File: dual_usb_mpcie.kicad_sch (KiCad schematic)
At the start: 28 parts, among them J1 91304-56-052R2, J2 91304-56-052R2, J3 USB, U1 AZ1117H-3.3, U2 AZ1117H-3.3, U3 AZ1117H-1.5, U4 AZ1117H-1.5

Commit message: Remove 1.5v. Change bottom pour to shield. Couple shield with ground. Add pull-up to W_DIS and PCIE_RST.
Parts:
- removed C5, C6: 22uF, Capacitor_SMD:C_1206_3216Metric, symbol Device:C_Polarized_Small_US
- removed FID1, FID2, FID3: Fiducial, parts:fiducial_jlcpcb_smt, symbol Mechanical:Fiducial
- removed U3, U4: AZ1117H-1.5, Package_TO_SOT_SMD:SOT-223-3_TabPin2, symbol Regulator_Linear:AZ1117-1.5
- added C5, C6, C7: 0.1uF, Capacitor_SMD:C_0603_1608Metric, symbol Device:C_Small
- added R3: 1M, Resistor_SMD:R_0603_1608Metric, symbol Device:R_Small_US
- added R4, R5, R6, R7: 3.3k, Resistor_SMD:R_0603_1608Metric, symbol Device:R_Small_US
- C1, C2, C3, C4: symbol Device:C_Polarized_Small_US -> Device:C_Small
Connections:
- net +3.3V_A: now also R6.1, R7.1
- net +3.3V_B: now also R4.1, R5.1
- net GND: now also C5.2, C6.2, C7.2, R3.2; no longer H1.1, H2.1, H3.1, H4.1
- net at J1.20 (~{W_DISABLE}): now also R6.2
- net at J1.22 (~{PERST}): now also C6.1, R7.2
- net at J2.20 (~{W_DISABLE}): now also R4.2
- net at J2.22 (~{PERST}): now also C5.1, R5.2
- net SHIELD: now reaches J3.10 (Pin_10)
- net SHIELD: now also H1.1, H2.1, H3.1, H4.1, C7.1, R3.1
- removed net +1.5V_A: J1.28 (+1V5), J1.48 (+1V5), J1.6 (+1V5)
- removed net +1.5V_B: J2.28 (+1V5), J2.48 (+1V5), J2.6 (+1V5)
- no-connect marks 52 -> 53

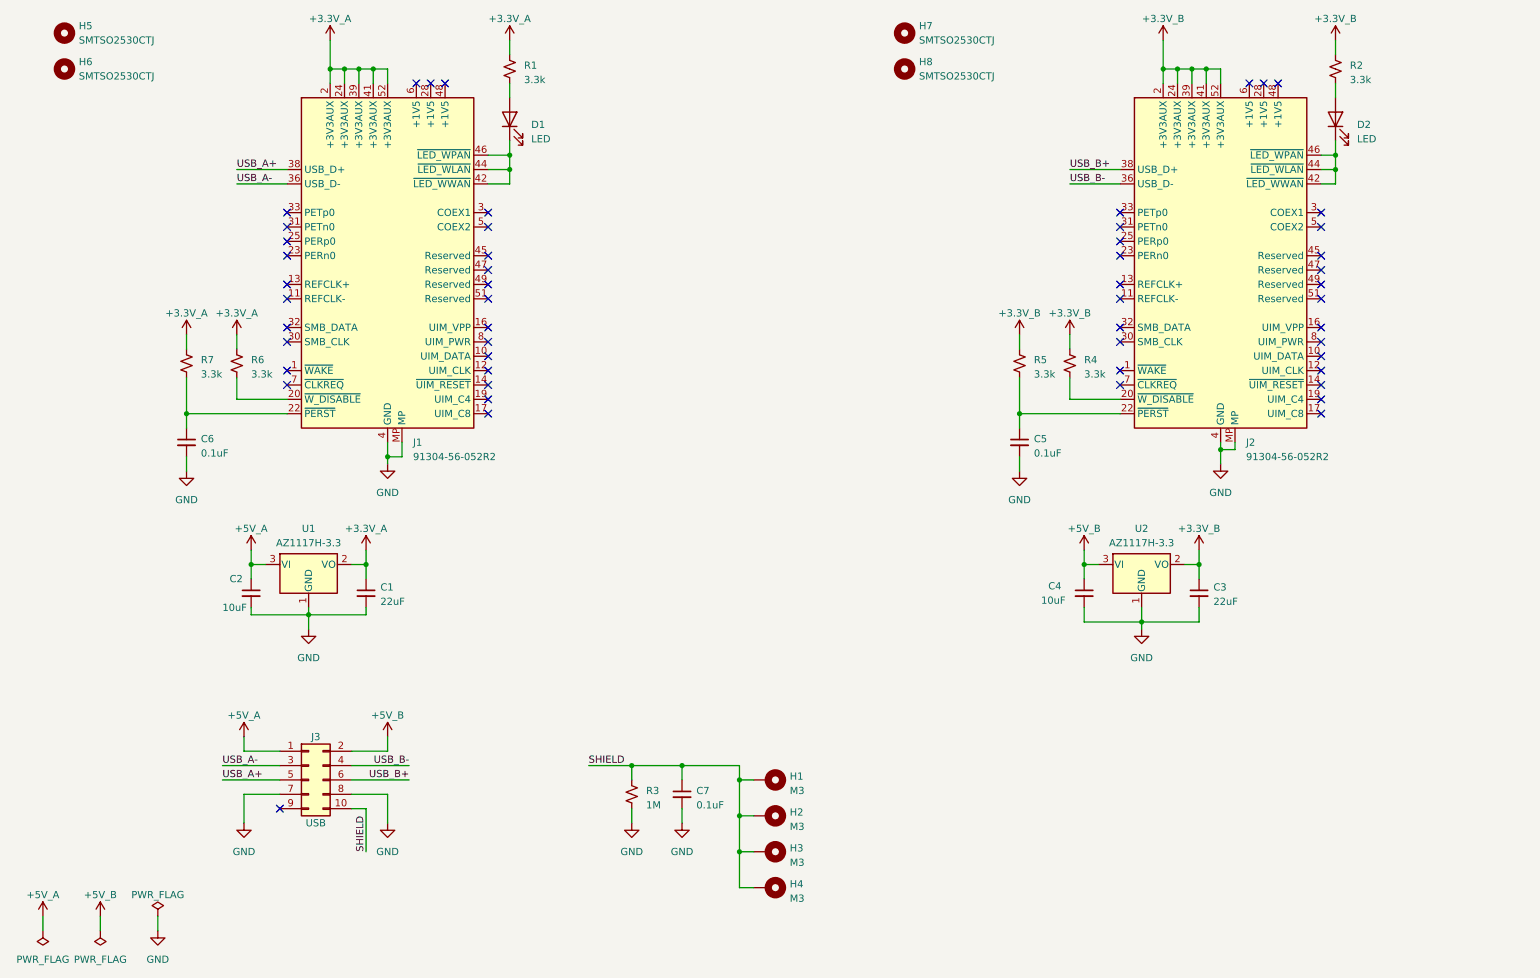
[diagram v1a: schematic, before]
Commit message: Rotate mpcie connectors so all routing is at the top of the board. Move power to the top. Move up mpcie connectors. Add silkscreen. Add models to mpcie and standoff
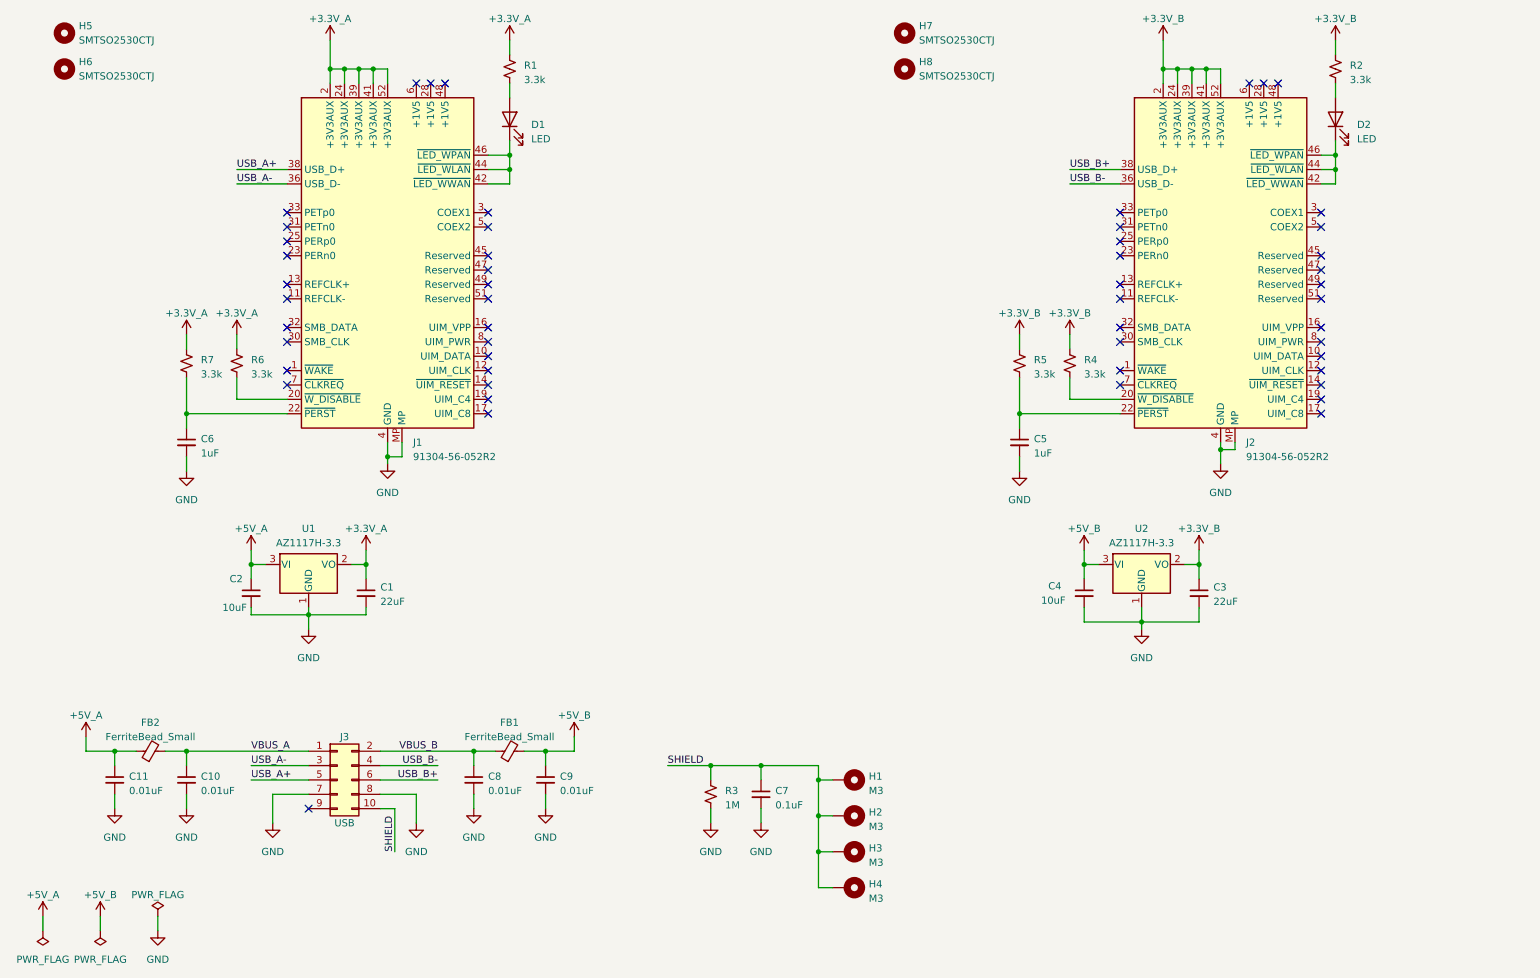
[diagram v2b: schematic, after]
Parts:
- added C10, C11, C8, C9: 0.01uF, Capacitor_SMD:C_0603_1608Metric, symbol Device:C_Small
- added FB1, FB2: FerriteBead_Small, Inductor_SMD:L_0603_1608Metric, symbol Device:FerriteBead_Small
- C5, C6: value 0.1uF -> 1uF; LCSC C14663 -> C15849
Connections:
- net +5V_A: now also C11.1, FB2.1; no longer J3.1 (Pin_1)
- net +5V_B: now also C9.1, FB1.2; no longer J3.2 (Pin_2)
- net GND: now also C10.2, C11.2, C8.2, C9.2
- new net VBUS_A: C10.1, FB2.2, J3.1 (Pin_1)
- new net VBUS_B: C8.1, FB1.1, J3.2 (Pin_2)
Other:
- moved on the sheet: C7, H1, H2, H3, H4, J3, R3

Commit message: Fix FB size for part. 0603 -> 0805
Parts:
- FB1, FB2: footprint Inductor_SMD:L_0603_1608Metric -> Inductor_SMD:L_0805_2012Metric
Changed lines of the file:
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@@
       (effects (font (size 1.27 1.27)))
     )
-    (property "Footprint" "Inductor_SMD:L_0603_1608Metric" (at 101.6 154.178 90)
+    (property "Footprint" "Inductor_SMD:L_0805_2012Metric" (at 101.6 154.178 90)
       (effects (font (size 1.27 1.27)) hide)
     )
@@
       (effects (font (size 1.27 1.27)))
     )
-    (property "Footprint" "Inductor_SMD:L_0603_1608Metric" (at 38.1 154.178 90)
+    (property "Footprint" "Inductor_SMD:L_0805_2012Metric" (at 38.1 154.178 90)
       (effects (font (size 1.27 1.27)) hide)
     )
